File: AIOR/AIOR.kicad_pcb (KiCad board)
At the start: 2 copper layers, 85 x 56.5 mm, 158 parts, among them J20 Conn_01x04, J30 Conn_01x02, J31 Conn_01x02, J50 Conn_01x02, J70 Conn_01x01, J81 Conn_01x06, J82 5V 12V, J90 Conn_01x03, P1 CONN_02X20, P2 CONN_01X02, P3 CAN, P50 XPN, P60 SLX, P70 LCN, P8 Conn_01x02, P9 Conn_01x04, Q30 BTN8982TA, Q31 BTN8982TA, Q60 BC817, Q70 BC817, Q90 BC857, Q91 BC857, U1 MCP2517FD, U2 ISO1050, U20 L7833, U21 L7805, U22 DSPIC33EP128GM604, U23 Si8605, U24 MCP2562, U4 P82B715, U40 C8051F502, U41 ADUM1251, U42 MCP2561, U50 MAX3072E, U70 LM393, U81 L7805, U82 SI8641-SOIC, U83 4504, U90 SAA6579, Y1 4MHz, Y20 8MHz, Y90 4MHz

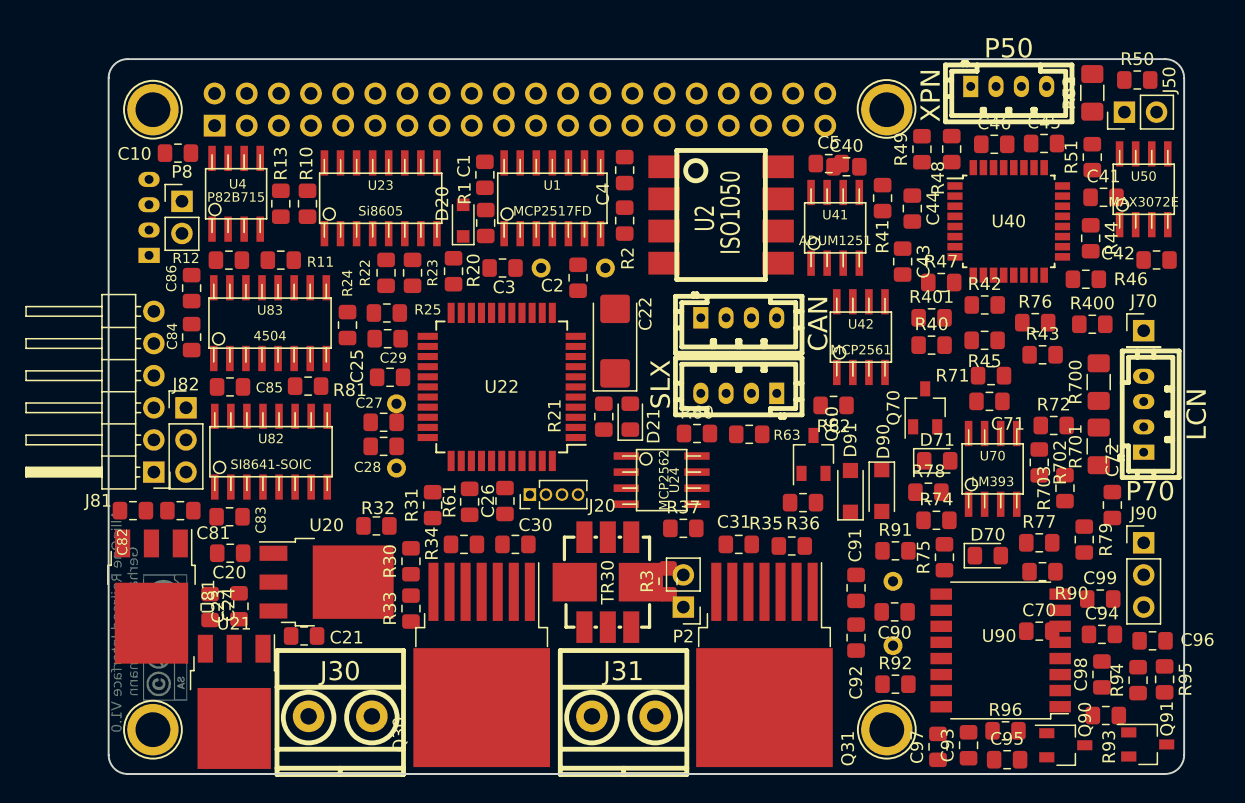
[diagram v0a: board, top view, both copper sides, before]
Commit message: optimize components placement
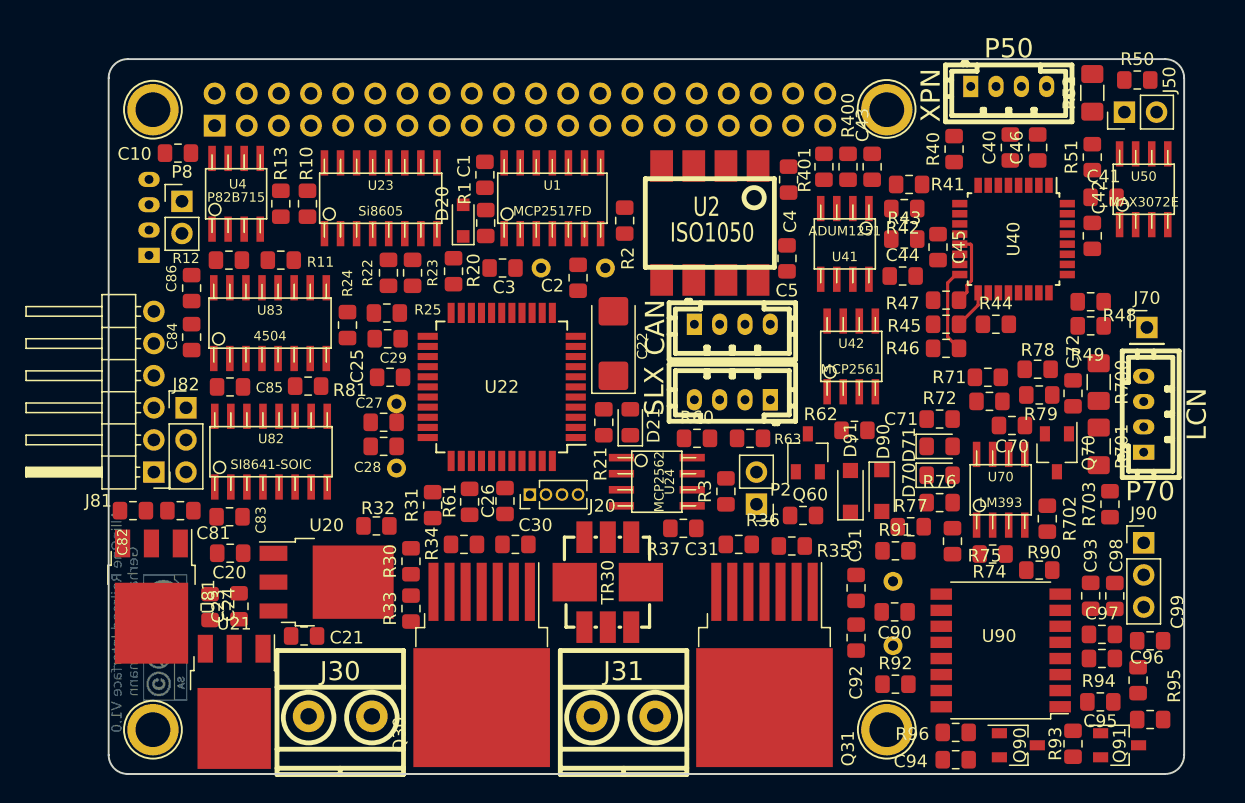
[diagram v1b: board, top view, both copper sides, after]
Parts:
- moved R400 23.0 mm to (186.4, 80.0), turned to 270 degrees
- moved R49 19.3 mm to (205.6, 92.6), turned to 180 degrees
- moved C70 16.4 mm to (199.4, 100.5), turned to 180 degrees
- moved R48 16.3 mm to (205.6, 90.7), turned to 180 degrees
- moved R76 16.1 mm to (193.7, 106.6)
- moved C97 15.7 mm to (206.5, 117.0), turned to 0 degrees
- moved R40 15.6 mm to (194.8, 78.6), turned to 90 degrees
- moved C93 15.3 mm to (205.6, 113.9)
- moved C94 15.2 mm to (194.9, 126.9)
- moved R401 14.7 mm to (184.5, 80.0), turned to 270 degrees
- moved R43 14.3 mm to (190.9, 85.7)
- moved C40 13.0 mm to (199.3, 78.5), turned to 90 degrees
- moved R78 13.0 mm to (201.4, 96.0), turned to 180 degrees
- moved C4 13.0 mm to (181.7, 81.0)
- moved R46 12.3 mm to (194.2, 94.4), turned to 180 degrees
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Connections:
- C5 pad 2: GND -> GNDA
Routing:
- net Net-(R46-Pad1): track 0.00 -> 6.78 mm
- net /B_SENSE: track 0.00 -> 5.71 mm
- net Net-(R45-Pad1): track 0.00 -> 3.11 mm

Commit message: wip
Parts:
- removed R92: 2k2, Resistor_SMD:R_0805_2012Metric_Pad1.15x1.40mm_HandSolder
- moved R71 21.9 mm to (189.6, 117.1)
- moved J70 20.9 mm to (211.6, 113.5)
- moved P70 20.7 mm to (210.2, 120.3)
- moved R79 20.0 mm to (203.9, 117.9)
- moved R78 19.1 mm to (203.8, 115.0)
- moved R703 19.0 mm to (206.1, 125.6), turned to 270 degrees
- moved Q70 18.8 mm to (203.9, 121.4)
- moved U70 17.9 mm to (199.4, 123.4)
- moved R93 17.9 mm to (205.9, 107.8), turned to 180 degrees
- moved R702 17.9 mm to (203.1, 125.7)
- moved R95 17.9 mm to (200.2, 109.0), turned to 0 degrees
- moved R700 17.7 mm to (207.0, 114.7)
- moved R701 17.7 mm to (207.0, 119.8)
- moved R72 17.6 mm to (194.7, 117.5)
- moved C95 17.5 mm to (195.1, 108.9), turned to 180 degrees
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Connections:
- C21 pad 1: +3V3 -> +3.3VA
- C25 pad 1: +3V3 -> +3.3VA
- C26 pad 1: +3V3 -> +3.3VA
- C27 pad 2: GND -> GNDA
- C28 pad 2: GND -> GNDA
- C82 pad 1: VCC -> VDDF
- C83 pad 1: +3V3 -> +3.3VA
- C84 pad 1: VCC -> VDDF
- C85 pad 1: VCC -> VDDF
- D20 pad 2: +3V3 -> +3.3VA
- D21 pad 2: +3V3 -> +3.3VA
- J82 pad 1: VCC -> VDDF
- P3 pad 1: GND -> GNDA
- R22 pad 1: +3V3 -> +3.3VA
- R23 pad 1: +3V3 -> +3.3VA
- U20 pad 3: +3V3 -> +3.3VA
- U22 pad 17: +3V3 -> +3.3VA
- U22 pad 28: +3V3 -> +3.3VA
- U22 pad 40: +3V3 -> +3.3VA
- U23 pad 1: +3V3 -> +3.3VA
- U24 pad 5: +3V3 -> +3.3VA
- U81 pad 3: VCC -> VDDF
- U82 pad 1: +3V3 -> +3.3VA
- U82 pad 16: VCC -> VDDF
- U83 pad 1: VCC -> VDDF
- U90 pad 14: Net-(R92-Pad2) -> Net-(C92-Pad1)
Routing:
- net +5VA: track 0.00 -> 187.6 mm, vias 0 -> 7
- net VCC: track 0.00 -> 103.7 mm, vias 0 -> 5
- net /B_ENA: track 0.00 -> 91.3 mm, vias 0 -> 6
- net +3V3: track 0.00 -> 83.7 mm
- net +3.3VA: track 0.00 -> 68.6 mm
- net /RS485_EN: track 0.00 -> 59.9 mm, vias 0 -> 2
- net /B_RIGHT: track 0.00 -> 57.5 mm, vias 0 -> 3
- net /RS485_TX: track 0.00 -> 54.8 mm, vias 0 -> 2
- net /RS485_RX: track 0.00 -> 53.3 mm, vias 0 -> 2
- net /LN_TX: track 0.00 -> 50.6 mm, vias 0 -> 2
- net Net-(Q30-Pad7): track 0.00 -> 47.7 mm, vias 0 -> 6
- net /SUBC: track 0.00 -> 38.8 mm
- net /LN_RX: track 0.00 -> 35.4 mm, vias 0 -> 2
- net /CANH: track 0.00 -> 32.8 mm
- net /B_SENSE: track 5.71 -> 35.8 mm, vias 0 -> 2
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- added copper zone on B.Cu, net GND
- added copper zone on F.Cu, net GND

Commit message: ready for V1.0
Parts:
- R3: footprint Resistor_SMD:R_0805_2012Metric_Pad1.15x1.40mm_HandSolder -> Resistor_SMD:R_1206_3216Metric_Pad1.42x1.75mm_HandSolder
- moved R32 17.7 mm to (146.8, 108.2)
- moved C42 4.08 mm to (205.9, 83.1)
- moved R49 3.42 mm to (202.2, 93.2)
- moved R90 1.92 mm to (200.2, 95.8), turned to 180 degrees
- moved R40 1.65 mm to (192.0, 79.8)
- moved C45 1.43 mm to (193.3, 85.1), turned to 90 degrees
- moved R47 1.38 mm to (192.5, 90.2)
- moved R48 0.93 mm to (206.5, 90.9)
- moved D90 0.68 mm to (189.1, 113.3)
- moved R41 0.63 mm to (191.3, 82.2)
- moved R79 0.52 mm to (203.9, 117.4)
- moved D91 0.46 mm to (186.7, 113.3)
- moved R78 0.45 mm to (203.8, 114.6)
- moved R3 0.43 mm to (176.6, 105.5)
- moved Q70 0.31 mm to (203.9, 121.1)
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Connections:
- P1 pad 14: Net-(P1-Pad14) -> GND
- P1 pad 20: Net-(P1-Pad20) -> GND
- P1 pad 25: Net-(P1-Pad25) -> GND
- P1 pad 30: Net-(P1-Pad30) -> GND
- P1 pad 34: Net-(P1-Pad34) -> GND
- U83 pad 13: VCC -> VDDF
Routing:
- net GNDA: track 0.35 -> 252.6 mm, vias 0 -> 50
- net /PGC: track 2.52 -> 79.3 mm, vias 0 -> 5
- net +5VA: track 187.6 -> 259.8 mm, vias 7 -> 14
- net /QUAL: track 12.0 -> 80.1 mm, vias 1 -> 3
- net /PGD: track 2.13 -> 70.2 mm, vias 0 -> 5
- net /B_SENSE: track 35.8 -> 96.1 mm, vias 2 -> 4
- net /RDDA: track 19.7 -> 75.9 mm, vias 2 -> 5
- net /RDCL: track 21.8 -> 72.4 mm, vias 0 -> 4
- net /Vccm: track 14.3 -> 63.0 mm, vias 0 -> 2
- net /B_LEFT: track 24.5 -> 64.3 mm, vias 2 -> 4
- net /SLX_DO: track 0.00 -> 39.6 mm, vias 0 -> 4
- net +3.3VA: track 68.6 -> 104.3 mm, vias 0 -> 5
- net /SLX_CL: track 0.00 -> 35.6 mm, vias 0 -> 4
- net Net-(U40-Pad28): track 0.00 -> 35.4 mm, vias 0 -> 2
- net Net-(U40-Pad27): track 0.00 -> 21.2 mm, vias 0 -> 2
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- added copper zone on B.Cu, net GNDA
- added copper zone on F.Cu, net GNDA
- added copper zone on B.Cu, net GNDS
- added copper zone on F.Cu, net GNDS

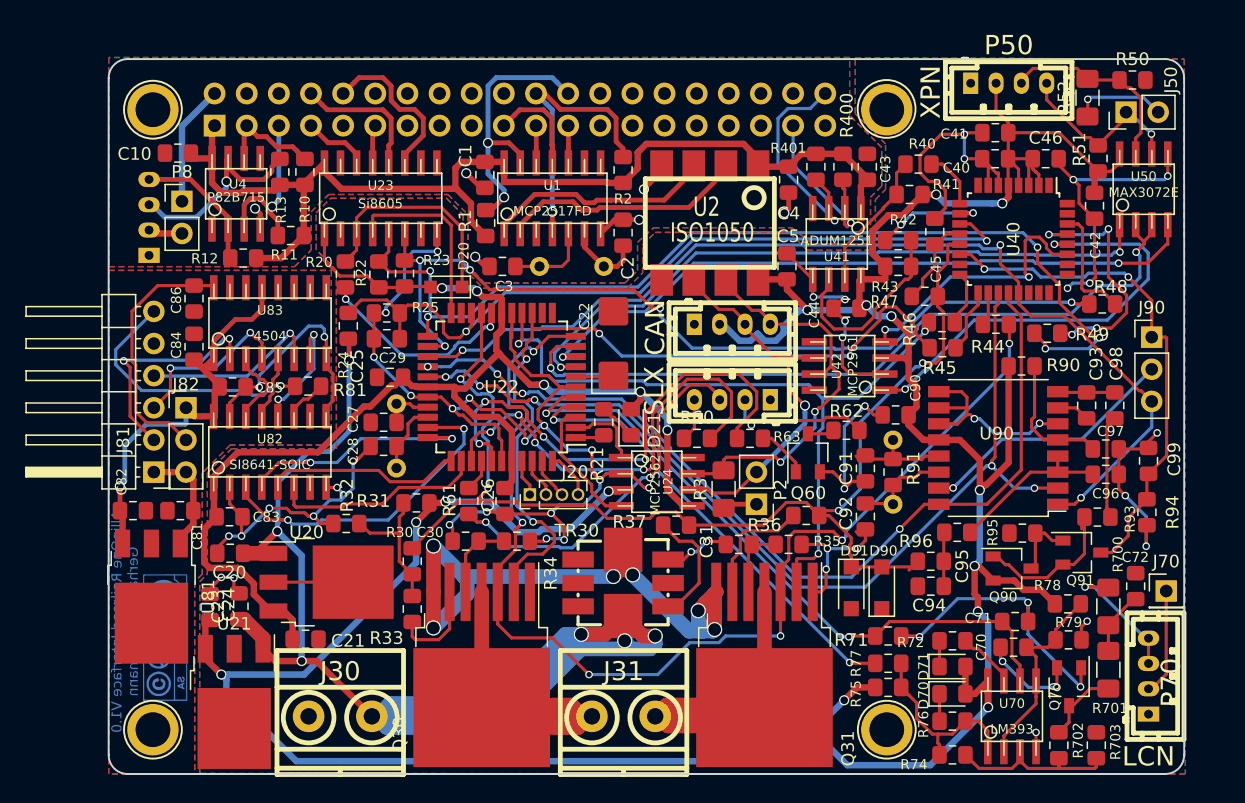
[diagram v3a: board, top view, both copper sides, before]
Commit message: vias shouldn't be on pads
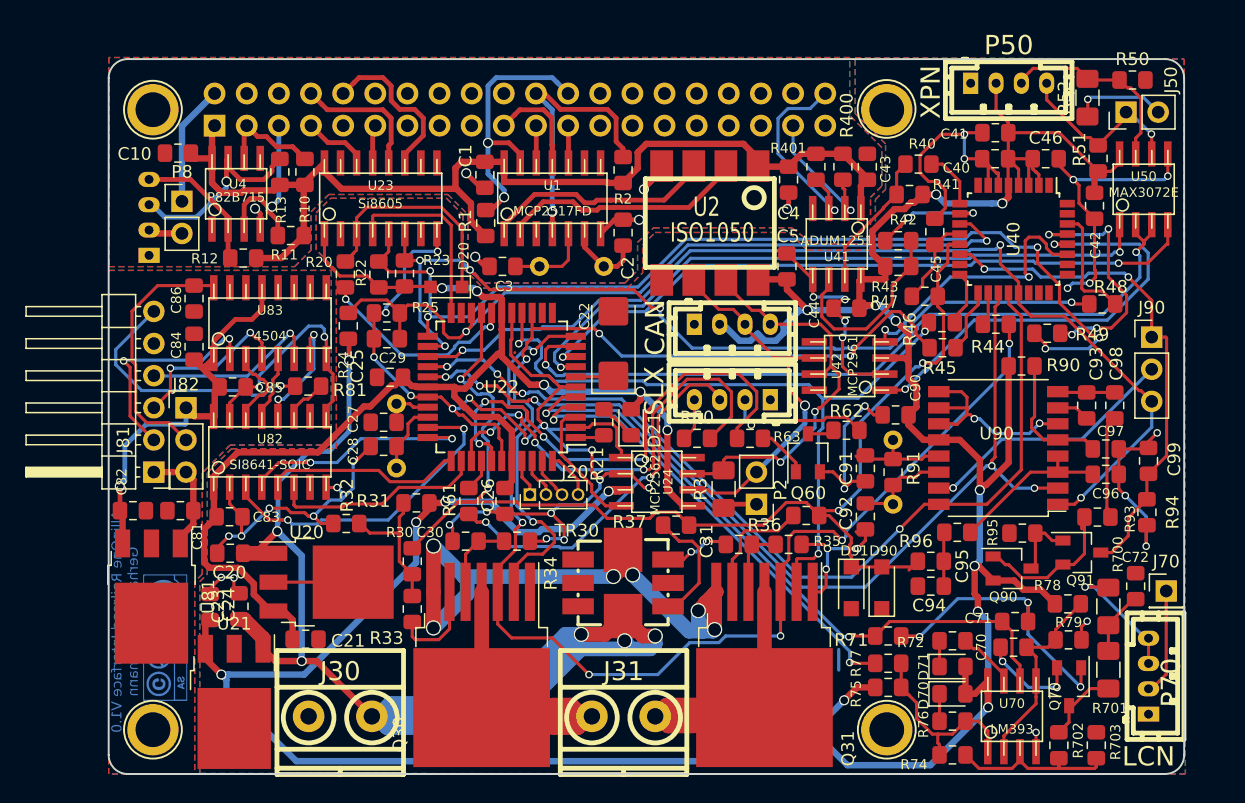
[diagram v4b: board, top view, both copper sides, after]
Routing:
- net /_C2D: track 13.9 -> 11.5 mm
- net (no net): track 0.00 -> 1.63 mm
- net GNDA: track 252.6 -> 253.9 mm
- net /_C2CK: track 18.3 -> 16.9 mm
- net /RS485_EN: track 60.1 -> 61.3 mm
- net /B_LEFT: track 64.3 -> 63.5 mm
- net Net-(R42-Pad1): track 9.11 -> 9.92 mm
- net +5VA: track 259.8 -> 260.4 mm

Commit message: change resitor for RS485
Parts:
- R50, R51: value 470 -> 4k7
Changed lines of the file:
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@@
-(kicad_pcb (version 20171130) (host pcbnew 5.1.2-f72e74a~84~ubuntu18.04.1)
+(kicad_pcb (version 20171130) (host pcbnew 5.1.2-f72e74a~84~ubuntu16.04.1)
   (general
     (thickness 1.6)
@@
       (effects (font (size 1 1) (thickness 0.15)))
     )
-    (fp_text value 470 (at 0 1.65) (layer F.Fab) hide
+    (fp_text value 4k7 (at 0 1.65) (layer F.Fab) hide
       (effects (font (size 1 1) (thickness 0.15)))
     )
@@
       (effects (font (size 1 1) (thickness 0.15)))
     )
-    (fp_text value 470 (at 0 1.65 90) (layer F.Fab) hide
+    (fp_text value 4k7 (at 0 1.65 90) (layer F.Fab) hide
       (effects (font (size 1 1) (thickness 0.15)))
     )

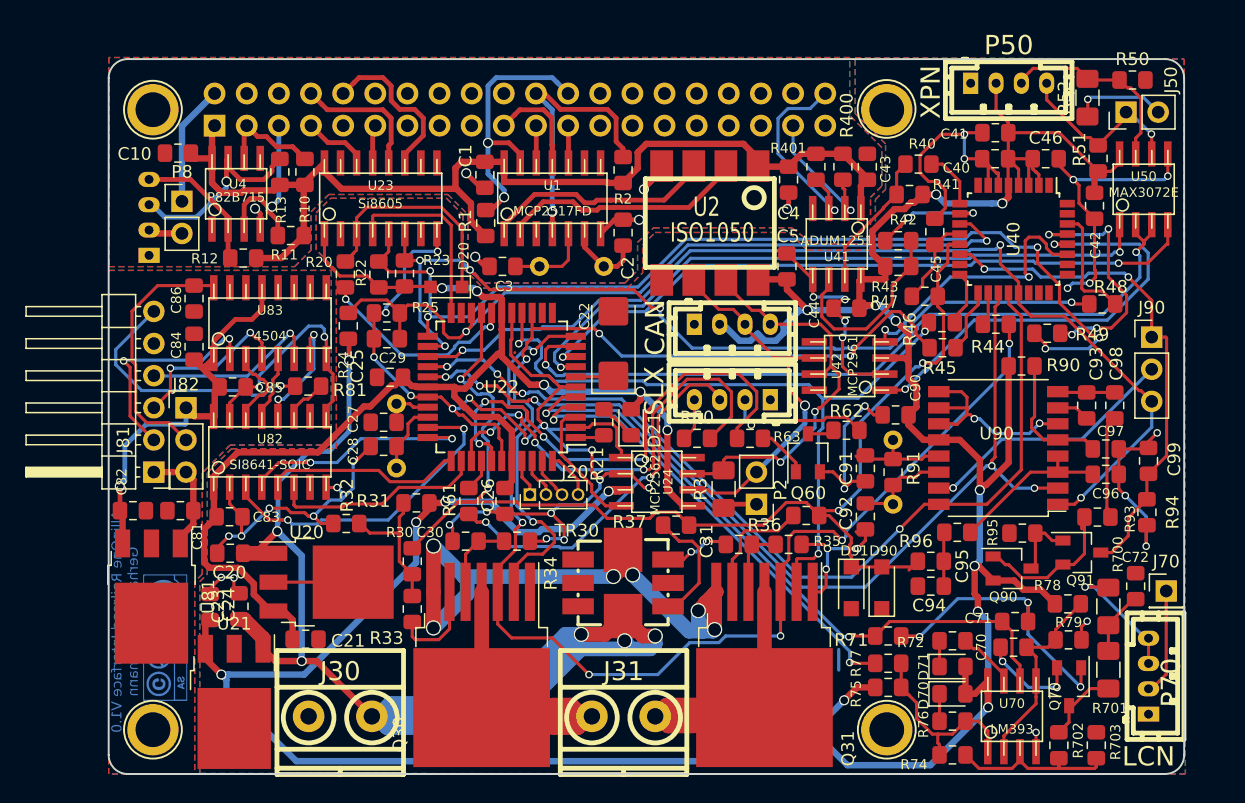
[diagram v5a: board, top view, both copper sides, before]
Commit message: fix RDS oscillator / use the right packages for regulators / small optimizations
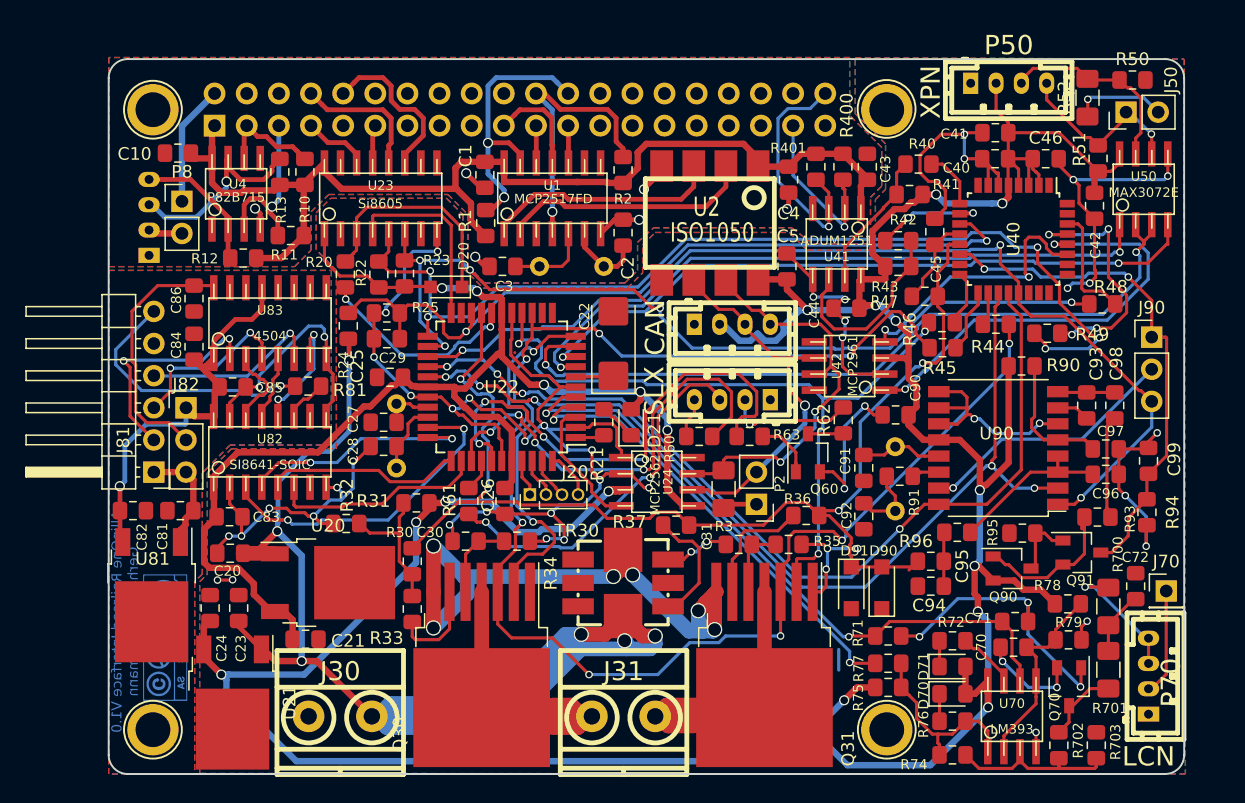
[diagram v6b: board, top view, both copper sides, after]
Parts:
- C92: value 47pF -> 82pF
- R91: value 1M -> 2k2
- U20, U21, U81: footprint Package_TO_SOT_SMD:TO-252-3_TabPin2 -> Package_TO_SOT_SMD:TO-252-2
- moved R62 0.83 mm to (186.1, 100.1), turned to 90 degrees
- moved R91 0.63 mm to (190.5, 104.5), turned to 0 degrees
- moved Y90 0.56 mm to (190.2, 104.7)
- moved R60 0.23 mm to (174.7, 101.3)
- moved R63 0.15 mm to (178.7, 101.3)
- moved C23 0.14 mm to (138.3, 114.9)
- moved U21 0.14 mm to (137.8, 122.4)
- moved C91 0.13 mm to (187.7, 103.8)
- moved C92 0.13 mm to (187.7, 107.6)
- moved U20 0.12 mm to (145.3, 112.9)
- moved U81 0.12 mm to (131.4, 113.9)
- moved C24 0.08 mm to (136.0, 114.9)
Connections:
- R91 pad 2: Net-(C91-Pad1) -> Net-(R91-Pad2)
- U90 pad 14: Net-(C92-Pad1) -> Net-(R91-Pad2)
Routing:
- net GNDA: track 253.9 -> 240.7 mm
- net Net-(R91-Pad2): track 0.00 -> 2.86 mm
- net Net-(C92-Pad1): track 8.39 -> 5.76 mm
- net /_C2CK: track 16.9 -> 19.3 mm
- net /_C2D: track 11.5 -> 13.7 mm
- net Net-(C91-Pad1): track 7.89 -> 6.51 mm
- net Net-(P60-Pad2): track 11.4 -> 10.1 mm
- net Net-(Q60-Pad1): track 4.11 -> 5.40 mm
- net Net-(Q60-Pad3): track 2.14 -> 2.82 mm
- net GND: track 13.2 -> 13.9 mm
- net +5VA: track 260.4 -> 260.9 mm
- net Net-(U1-Pad2): track 19.7 -> 20.2 mm
- net Net-(U1-Pad1): track 18.4 -> 18.9 mm
